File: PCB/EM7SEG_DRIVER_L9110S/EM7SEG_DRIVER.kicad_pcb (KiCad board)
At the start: 2 copper layers, 27 x 38.8 mm, 40 parts, among them J1 I2C_PWR_IN, J2 I2C_PWR_OUT, U1 EM7SEG, U2 MCP23017_SP, U3 L9110S, U4 L9110S, U5 L9110S, U6 L9110S, U7 L9110S, U8 L9110S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

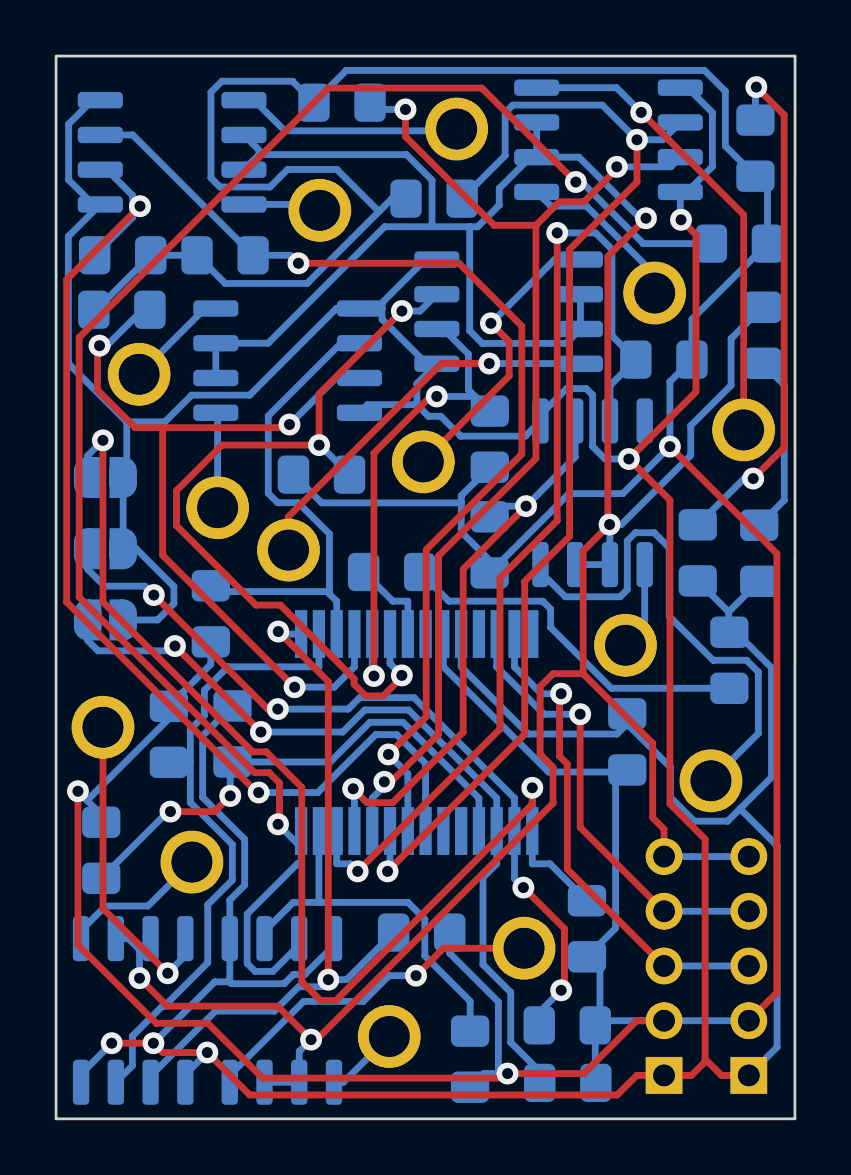
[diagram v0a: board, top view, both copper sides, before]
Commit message: use pull-downs instead of pull-ups for l9110 inputs
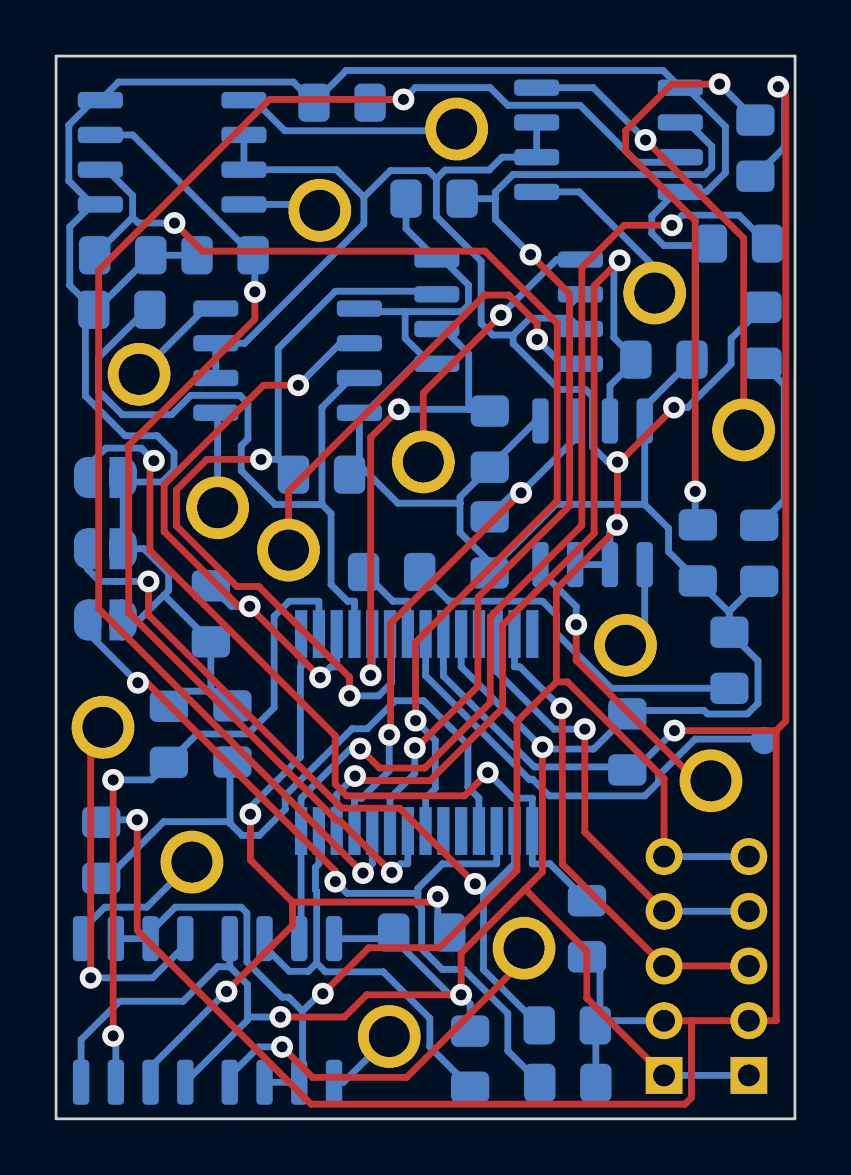
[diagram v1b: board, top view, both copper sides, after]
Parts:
- added J3: Pad_IO16, TestPoint:TestPoint_Pad_D1.0mm, B.Cu at (51.5, 51.6)
- turned R14 to 90 degrees
- turned R15 to 180 degrees
- turned R16 to 180 degrees
- turned R21 to 0 degrees
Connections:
- R10 pad 2: +5V -> GND
- R11 pad 2: +5V -> GND
- R12 pad 2: +5V -> GND
- R13 pad 2: +5V -> GND
- R14 pad 2: +5V -> GND
- R15 pad 2: +5V -> GND
- R16 pad 2: +5V -> GND
- R17 pad 2: +5V -> GND
- R18 pad 2: +5V -> GND
- R19 pad 2: +5V -> GND
- R20 pad 2: +5V -> GND
- R21 pad 2: +5V -> GND
- R8 pad 2: +5V -> GND
- R9 pad 2: +5V -> GND
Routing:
- net +5V: track 175.8 -> 96.4 mm
- net IN_D2: track 60.0 -> 39.4 mm
- net Net-(J3-Pad1): track 0.00 -> 16.7 mm
- net IN_B2: track 39.6 -> 54.2 mm, vias 3 -> 2
- net GND: track 182.8 -> 193.9 mm, vias 5 -> 3
- net Net-(JP1-Pad1): track 42.3 -> 31.2 mm
- net +12V: track 115.5 -> 105.0 mm
- net C2: track 18.9 -> 10.8 mm, vias 0 -> 1
- net IN_F1: track 18.3 -> 22.6 mm, vias 0 -> 3
- net IN_B1: track 43.1 -> 39.0 mm
- net IN_C2: track 37.7 -> 33.7 mm
- net RESET: track 19.2 -> 23.0 mm, vias 2 -> 0
- net IN_F2: track 30.1 -> 26.8 mm, vias 3 -> 0
- net G2: track 14.2 -> 17.2 mm
- net IN_A1: track 40.0 -> 42.6 mm
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
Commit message: update kicad version
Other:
- net class Default removed
